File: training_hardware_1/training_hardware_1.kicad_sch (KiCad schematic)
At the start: 0 parts

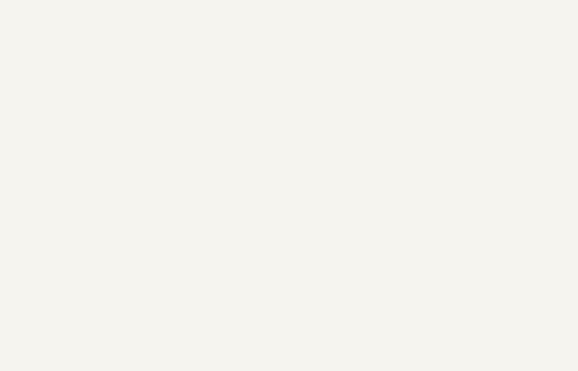
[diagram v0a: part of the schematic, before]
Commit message: Add CAN Transceiver
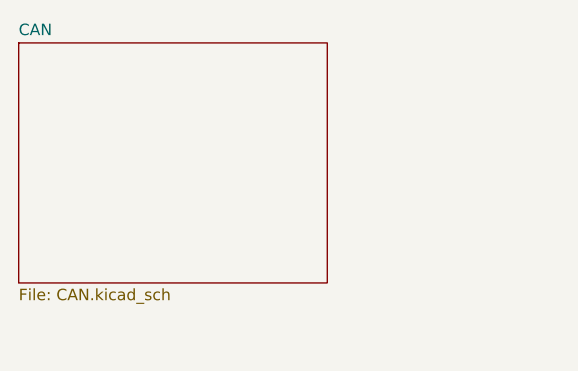
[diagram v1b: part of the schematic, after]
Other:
- added sheet CAN (CAN.kicad_sch)
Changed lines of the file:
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@@
 	(paper "A4")
+	(sheet
+		(at 29.21 100.33)
+		(size 34.29 26.67)
+		(exclude_from_sim no)
+		(in_bom yes)
+		(on_board yes)
+		(dnp no)
+		(fields_autoplaced yes)
+		(stroke
+			(width 0.1524)
+			(type solid)
+		)
+		(fill
+			(color 0 0 0 0.0000)
+		)
+		(property "Sheetname" "CAN"
+			(at 29.21 99.6184 0)
+			(effects
+				(font
+					(size 1.27 1.27)
+				)
+				(justify left bottom)
+			)
+		)
+		(property "Sheetfile" "CAN.kicad_sch"
+			(at 29.21 127.5846 0)
+			(effects
+				(font
+					(size 1.27 1.27)
+				)
+				(justify left top)
+			)
+		)
+		(instances
+			(project "training_hardware_1"
+				(path "/7ad66101-d49b-4767-9ce8-b98c98937367"
+					(page "4")
+				)
+			)
+		)
+	)
 	(sheet
 		(at 190.5 106.68)

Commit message: Finish Schematic
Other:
- sheet CAN ports: added RXD, STBY, TXD; removed none
- sheet MCU ports: added CRX1, CTX1, STBY; removed none
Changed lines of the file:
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@@
 	(generator_version "9.0")
 	(paper "A4")
+	(wire
+		(pts
+			(xy 63.5 106.68) (xy 92.71 106.68)
+		)
+		(stroke
+			(width 0)
+			(type default)
+		)
+	)
+	(wire
+		(pts
+			(xy 63.5 111.76) (xy 92.71 111.76)
+		)
+		(stroke
+			(width 0)
+			(type default)
+		)
+	)
+	(wire
+		(pts
+			(xy 63.5 115.57) (xy 92.71 115.57)
+		)
+		(stroke
+			(width 0)
+			(type default)
+		)
+	)
 	(sheet
 		(at 29.21 100.33)
@@
 				)
 				(justify left top)
+			)
+		)
+		(pin "RXD" output
+			(at 63.5 106.68 0)
+			(effects
+				(font
+					(size 1.27 1.27)
+				)
+				(justify right)
+			)
+		)
+		(pin "STBY" input
+			(at 63.5 111.76 0)
+			(effects
+				(font
+					(size 1.27 1.27)
+				)
+				(justify right)
+			)
+		)
+		(pin "TXD" input
+			(at 63.5 115.57 0)
+			(effects
+				(font
+					(size 1.27 1.27)
+				)
+				(justify right)
 			)
 		)
@@
 			)
 		)
+		(pin "CRX1" input
+			(at 92.71 106.68 180)
+			(effects
+				(font
+					(size 1.27 1.27)
+				)
+				(justify left)
+			)
+		)
+		(pin "CTX1" input
+			(at 92.71 115.57 180)
+			(effects
+				(font
+					(size 1.27 1.27)
+				)
+				(justify left)
+			)
+		)
+		(pin "STBY" output
+			(at 92.71 111.76 180)
+			(effects
+				(font
+					(size 1.27 1.27)
+				)
+				(justify left)
+			)
+		)

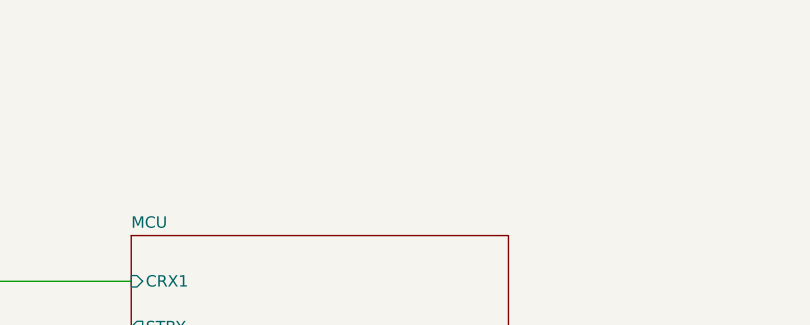
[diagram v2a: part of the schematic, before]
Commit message: Add components and wires(1:28)
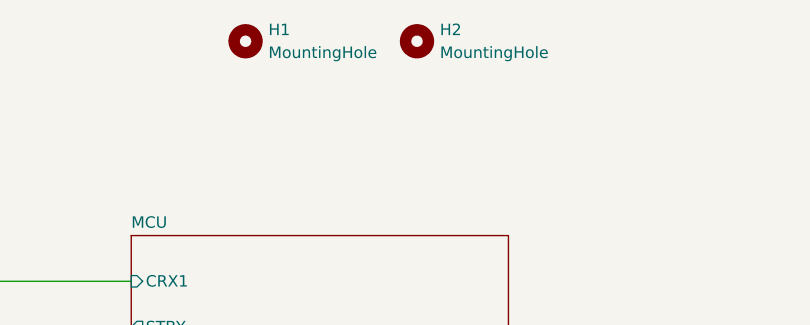
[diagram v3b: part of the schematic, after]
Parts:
- added H1, H2: MountingHole, MRDT_Drill_Holes:4_40_Hole_Corner, symbol Mechanical:MountingHole
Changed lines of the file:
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@@
+		)
+	)
+	(symbol
+		(lib_id "Mechanical:MountingHole")
+		(at 105.41 80.01 0)
+		(unit 1)
+		(exclude_from_sim no)
+		(in_bom no)
+		(on_board yes)
+		(dnp no)
+		(fields_autoplaced yes)
+		(property "Reference" "H1"
+			(at 107.95 78.7399 0)
+			(effects
+				(font
+					(size 1.27 1.27)
+				)
+				(justify left)
+			)
+		)
+		(property "Value" "MountingHole"
+			(at 107.95 81.2799 0)
+			(effects
+				(font
+					(size 1.27 1.27)
+				)
+				(justify left)
+			)
+		)
+		(property "Footprint" "MRDT_Drill_Holes:4_40_Hole_Corner"
+			(at 105.41 80.01 0)
+			(effects
+				(font
+					(size 1.27 1.27)
+				)
+				(hide yes)
+			)
+		)
+		(property "Datasheet" "~"
+			(at 105.41 80.01 0)
+			(effects
+				(font
+					(size 1.27 1.27)
+				)
+				(hide yes)
+			)
+		)
+		(property "Description" "Mounting Hole without connection"
+			(at 105.41 80.01 0)
+			(effects
+				(font
+					(size 1.27 1.27)
+				)
+				(hide yes)
+			)
+		)
+		(instances
+			(project ""
+				(path "/7ad66101-d49b-4767-9ce8-b98c98937367"
+					(reference "H1")
+					(unit 1)
+				)
+			)
+		)
+	)
+	(symbol
+		(lib_id "Mechanical:MountingHole")
+		(at 124.46 80.01 0)
+		(unit 1)
+		(exclude_from_sim no)
+		(in_bom no)
+		(on_board yes)
+		(dnp no)
+		(fields_autoplaced yes)
+		(property "Reference" "H2"
+			(at 127 78.7399 0)
+			(effects
+				(font
+					(size 1.27 1.27)
+				)
+				(justify left)
+			)
+		)
+		(property "Value" "MountingHole"
+			(at 127 81.2799 0)
+			(effects
+				(font
+					(size 1.27 1.27)
+				)
+				(justify left)
+			)
+		)
+		(property "Footprint" "MRDT_Drill_Holes:4_40_Hole_Corner"
+			(at 124.46 80.01 0)
+			(effects
+				(font
+					(size 1.27 1.27)
+				)
+				(hide yes)
+			)
+		)
+		(property "Datasheet" "~"
+			(at 124.46 80.01 0)
+			(effects
+				(font
+					(size 1.27 1.27)
+				)
+				(hide yes)
+			)
+		)
+		(property "Description" "Mounting Hole without connection"
+			(at 124.46 80.01 0)
+			(effects
+				(font
+					(size 1.27 1.27)
+				)
+				(hide yes)
+			)
+		)
+		(instances
+			(project "training_hardware_1"
+				(path "/7ad66101-d49b-4767-9ce8-b98c98937367"
+					(reference "H2")
+					(unit 1)
+				)
+			)
 		)
 	)
